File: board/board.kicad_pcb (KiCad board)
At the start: 2 copper layers, 21 x 45 mm, 13 parts, among them J1 001_I2C, J2 007_ADC, J3 001_I2C, J4 007_ADC, U1 MCP3428

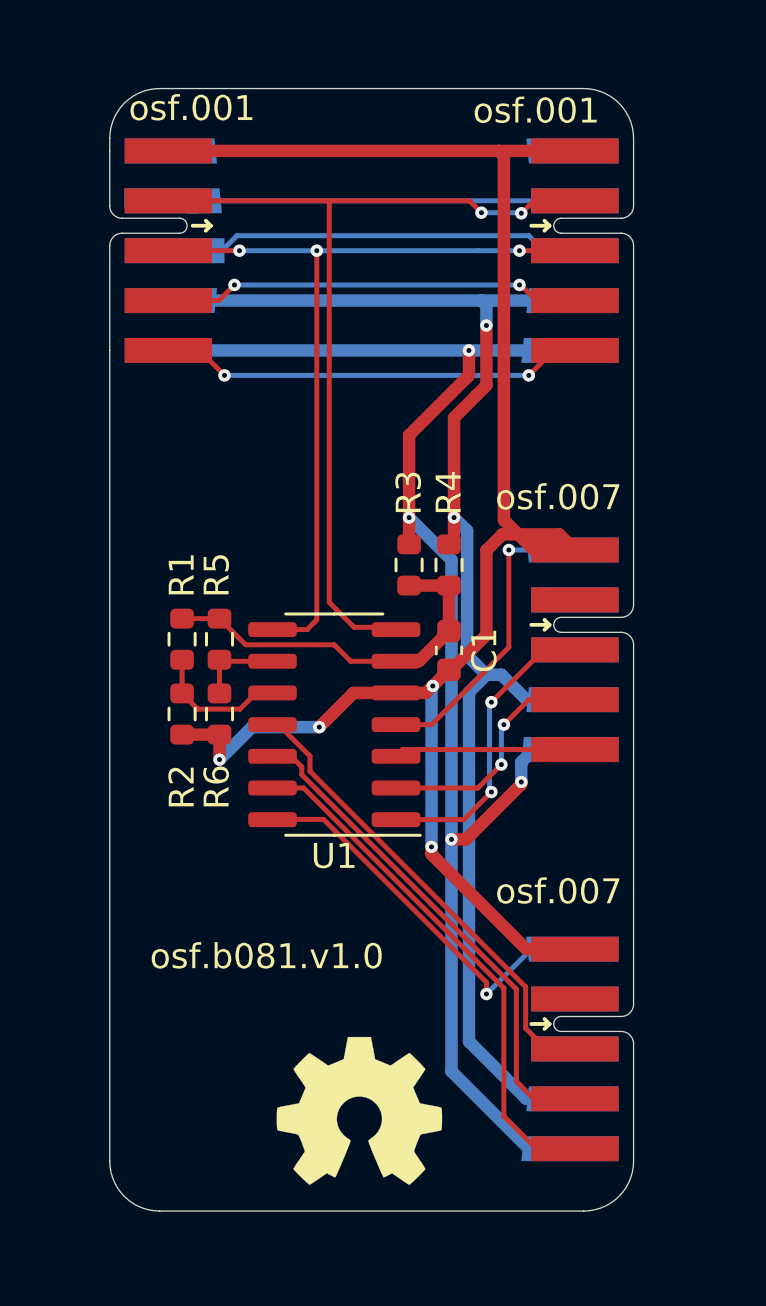
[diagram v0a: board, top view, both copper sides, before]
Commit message: added copper pours and moved edgy specific components out of the subsheet
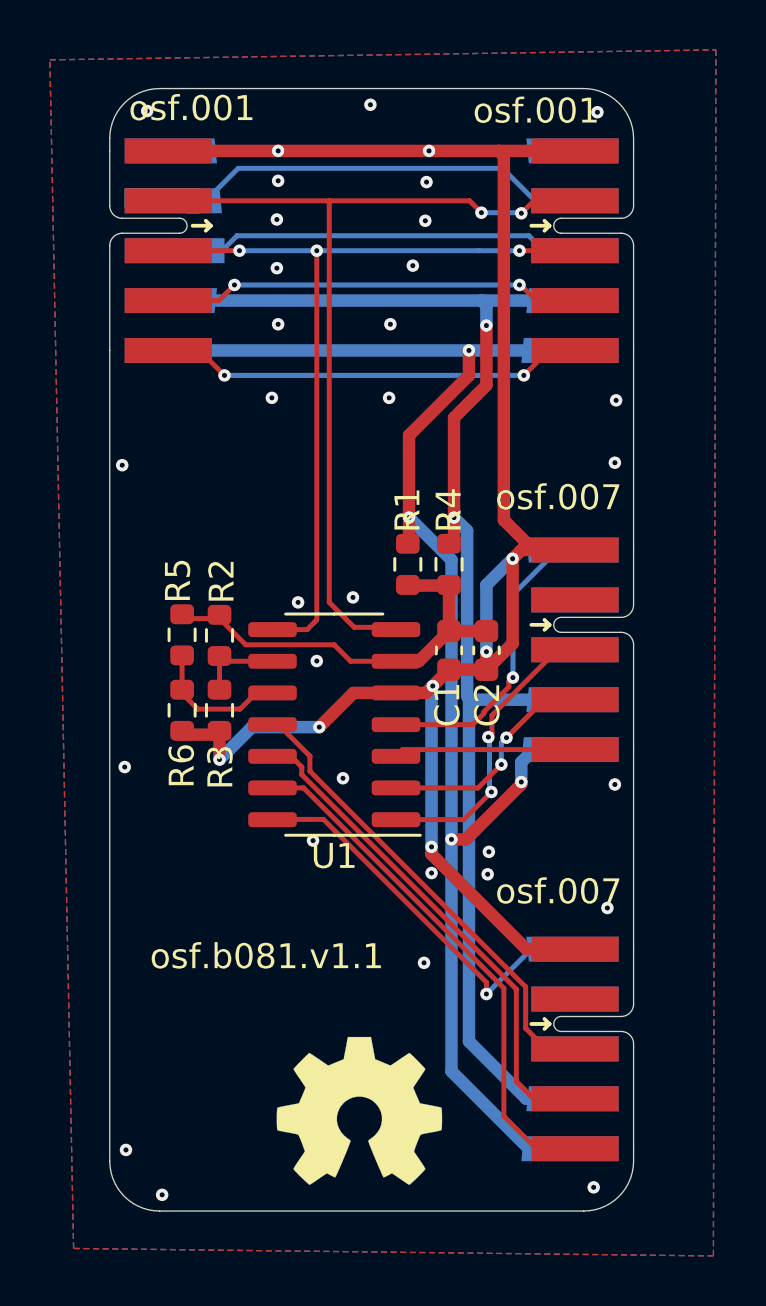
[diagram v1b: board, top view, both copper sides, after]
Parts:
- added C2: 10uF, Capacitor_SMD:C_0603_1608Metric, F.Cu at (155.1, 112.5)
- R1: value d.n.p -> 0R
- R2: value 0R -> d.n.p
- moved R3 9.58 mm to (144.4, 114.9), turned to -90 degrees
- moved R1 9.53 mm to (151.9, 109.1)
- moved R2 3.49 mm to (144.4, 111.9), turned to 90 degrees
- moved R5 1.51 mm to (142.9, 111.9)
- moved R6 1.51 mm to (142.9, 114.9)
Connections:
- C1 pad 1: Net-(C1-Pad1) -> /adc/VDD
- R1 pad 1: Net-(U1-Pad10) -> /adc/VDD
- R1 pad 2: Net-(C1-Pad1) -> /5V
- R2 pad 1: Net-(U1-Pad10) -> /adc/AD0
- R2 pad 2: GND -> /adc/VDD
- R3 pad 1: Net-(C1-Pad1) -> /adc/AD0
- R3 pad 2: /5V -> GND
- R4 pad 1: Net-(C1-Pad1) -> /adc/VDD
- R5 pad 1: Net-(U1-Pad9) -> /adc/AD1
- R5 pad 2: Net-(C1-Pad1) -> /adc/VDD
- R6 pad 2: Net-(U1-Pad9) -> /adc/AD1
- U1 pad 10: Net-(U1-Pad10) -> /adc/AD1
- U1 pad 6: Net-(C1-Pad1) -> /adc/VDD
- U1 pad 9: Net-(U1-Pad9) -> /adc/AD0
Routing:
- net /adc/VDD: track 0.00 -> 16.8 mm
- net Net-(C1-Pad1): track 15.3 -> 0.00 mm
- net Net-(U1-Pad10): track 5.03 -> 0.00 mm
- net /adc/AD1: track 0.00 -> 5.03 mm
- net Net-(U1-Pad9): track 3.50 -> 0.00 mm
- net /adc/AD0: track 0.00 -> 3.50 mm
- net GND: track 71.4 -> 74.1 mm, vias 4 -> 39
- net (no net): track 16.6 -> 17.6 mm
- added copper zone on B.Cu, net GND
- added copper zone on F.Cu, net GND
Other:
- board text added: "osf.b081.v1.1"
- board text removed: "osf.b081.v1.0"
